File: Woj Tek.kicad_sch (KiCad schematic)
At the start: 4 parts, among them J2 Conn_01x02, J3 Conn_01x02, J4 Conn_01x02

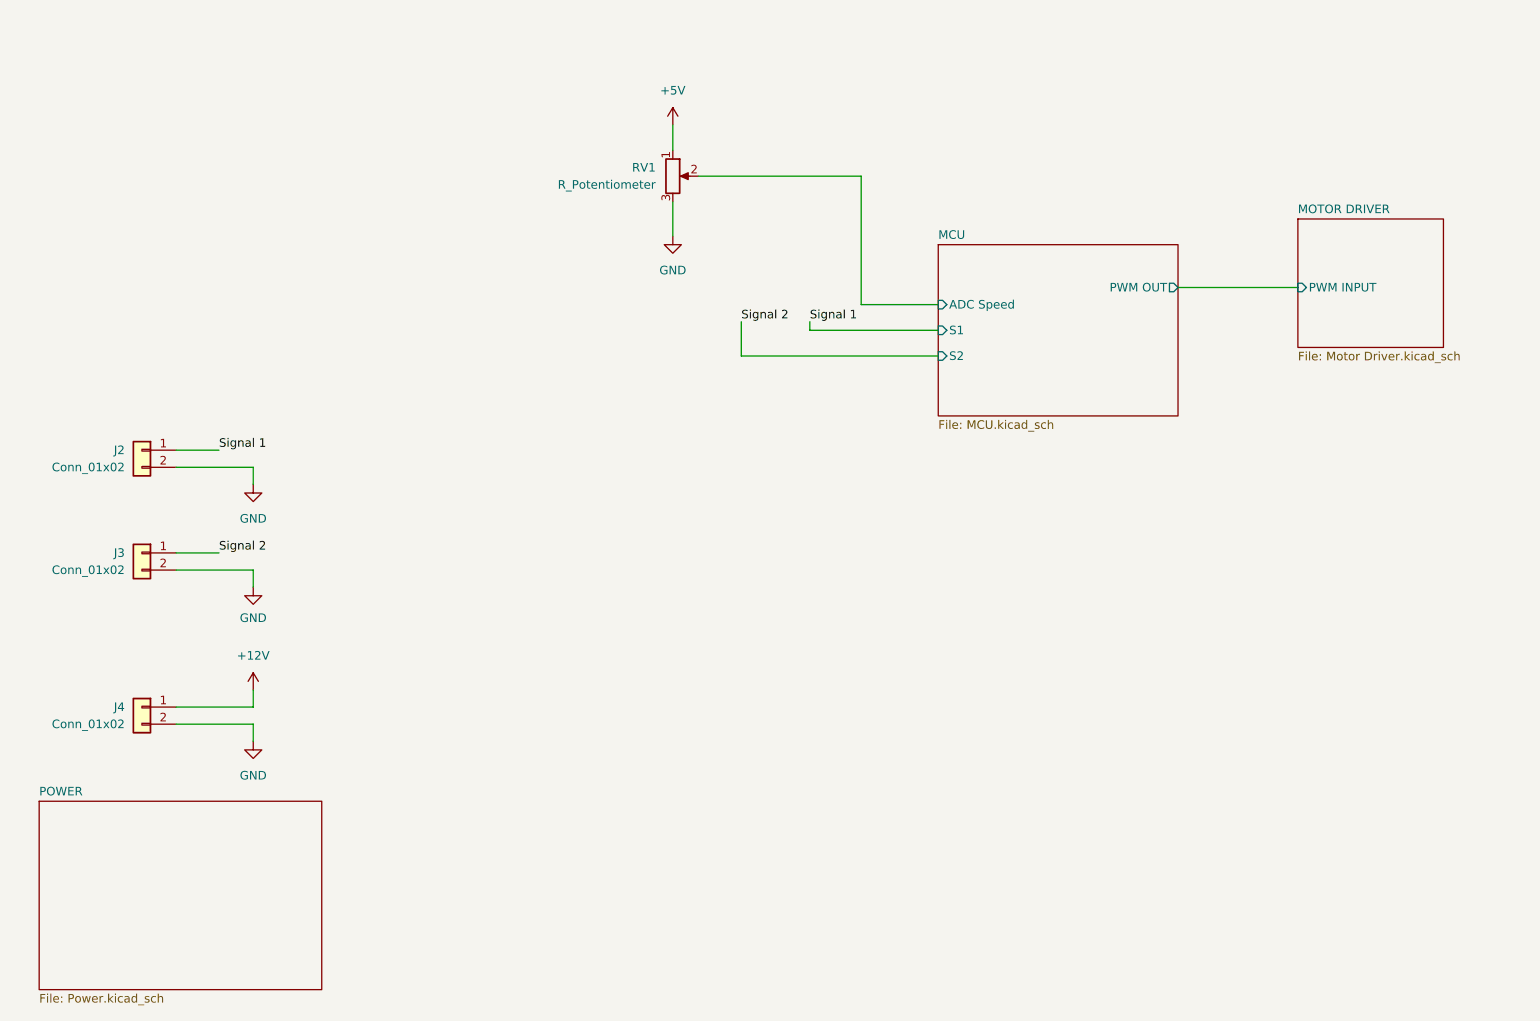
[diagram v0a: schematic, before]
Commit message: Correction in designators.
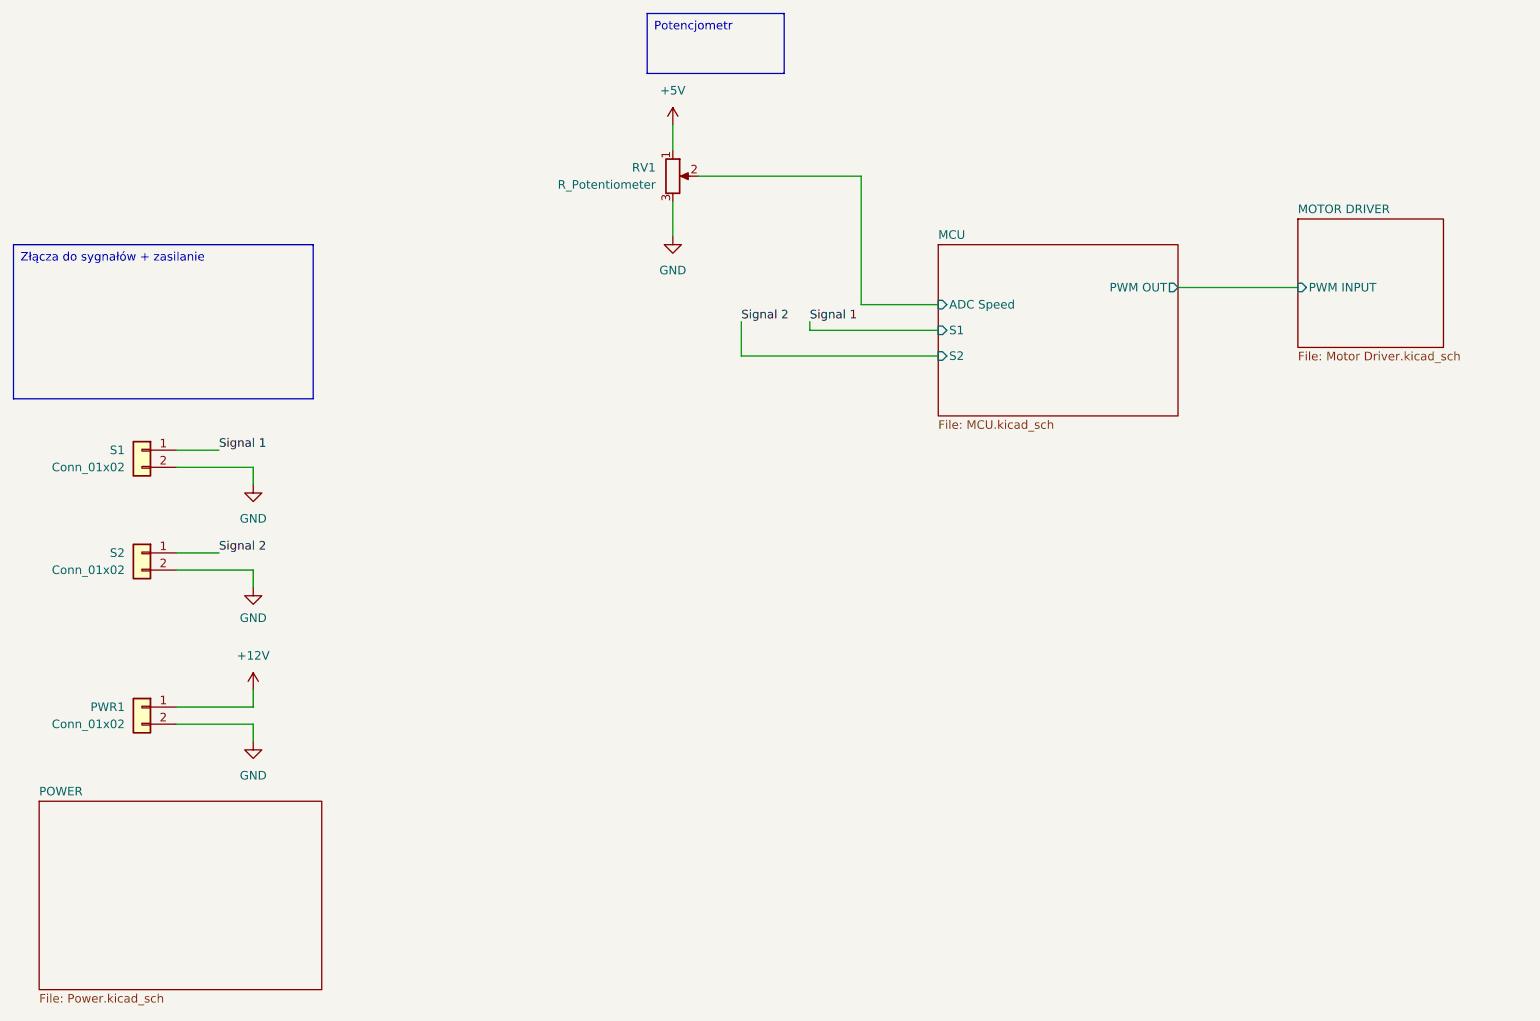
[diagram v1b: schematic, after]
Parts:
- renumbered J4 to PWR1, J2 to S1, J3 to S2
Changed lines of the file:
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@@
+		)
+	)
+	(text_box "Potencjometr\n\n"
+		(exclude_from_sim no)
+		(at 118.11 35.56 0)
+		(size 20.32 8.89)
+		(stroke
+			(width 0)
+			(type default)
+		)
+		(fill
+			(type none)
+		)
+		(effects
+			(font
+				(size 1.27 1.27)
+			)
+			(justify left top)
+		)
+	)
+	(text_box "Złącza do sygnałów + zasilanie"
+		(exclude_from_sim no)
+		(at 24.13 69.85 0)
+		(size 44.45 22.86)
+		(stroke
+			(width 0)
+			(type default)
+		)
+		(fill
+			(type none)
+		)
+		(effects
+			(font
+				(size 1.27 1.27)
+			)
+			(justify left top)
 		)
 	)
@@
 		(on_board yes)
 		(dnp no)
-		(property "Reference" "J4"
+		(property "Reference" "PWR1"
 			(at 40.64 138.4299 0)
 			(effects
@@
 			(project "Woj Tek"
 				(path "/99eb6018-140e-4249-b7a3-7c5f4275a21b"
-					(reference "J4")
+					(reference "PWR1")
 					(unit 1)
 				)
@@
 		(on_board yes)
 		(dnp no)
-		(property "Reference" "J2"
+		(property "Reference" "S1"
 			(at 40.64 100.3299 0)
 			(effects
@@
 			(project ""
 				(path "/99eb6018-140e-4249-b7a3-7c5f4275a21b"
-					(reference "J2")
+					(reference "S1")
 					(unit 1)
 				)
@@
 		(on_board yes)
 		(dnp no)
-		(property "Reference" "J3"
+		(property "Reference" "S2"
 			(at 40.64 115.5699 0)
 			(effects
@@
 			(project "Woj Tek"
 				(path "/99eb6018-140e-4249-b7a3-7c5f4275a21b"
-					(reference "J3")
+					(reference "S2")
 					(unit 1)
 				)
